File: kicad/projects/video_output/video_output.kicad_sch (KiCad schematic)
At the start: 70 parts, among them J1 peripheral_addr_bus_connector, J2 peripheral_aux_connector, J3 peripheral_membank_connector, J4 Conn_01x16_Socket, J5 Conn_01x16_Socket, J6 Conn_02x06_Odd_Even, J7 DE15_Receptacle_HighDensity, J8 video_aux, J9 Conn_01x04_Socket, U1 628128_DIP32_SSOP32, U10 74HC157, U11 74HC157, U12 74HC10, U13 74HC02, U14 74HC08, U15 74HC123, U16 74HC32, U17 74HC04, U2 628128_DIP32_SSOP32, U3 74HC245, U4 74HC245, U5 74HC245, U6 74HC245, U7 74HC574, U8 74HC245, U9 74HC574

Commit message: First pass of output PCB complete.
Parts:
- removed J7: DE15_Receptacle_HighDensity, Connector_Dsub:DSUB-15_Female_Horizontal_P2.77x2.84mm_EdgePinOffset9.90mm_Housed_MountingHolesOffset11.32mm, symbol Connector:DE15_Receptacle_HighDensity
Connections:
- net PIX_A_B_00: now also U2.14 (Q1), U3.14 (B5), U5.14 (B5); no longer U2.18 (Q4), U3.17 (B2), U5.17 (B2)
- net PIX_A_B_01: now also U2.13 (Q0), U3.13 (B6), U5.13 (B6); no longer U2.19 (Q5), U3.18 (B1), U5.18 (B1)
- net PIX_A_G_00: now also U2.17 (Q3), U3.16 (B3), U5.16 (B3); no longer U2.15 (Q2), U3.15 (B4), U5.15 (B4)
- net PIX_A_G_01: now also U2.15 (Q2), U3.15 (B4), U5.15 (B4); no longer U2.17 (Q3), U3.16 (B3), U5.16 (B3)
- net PIX_A_R_00: now also U2.19 (Q5), U3.18 (B1), U5.18 (B1); no longer U2.13 (Q0), U3.13 (B6), U5.13 (B6)
- net PIX_A_R_01: now also U2.18 (Q4), U3.17 (B2), U5.17 (B2); no longer U2.14 (Q1), U3.14 (B5), U5.14 (B5)
- net PIX_B_00: now also U9.18 (Q1); no longer U9.15 (Q4)
- net PIX_B_00_CLOCKED: now also RN5.8 (R7), U8.17 (B2), U9.3 (D1); no longer RN5.5 (R4), U8.14 (B5), U9.6 (D4)
- net PIX_B_00_OUT: now also R10.1, U8.3 (A2); no longer R14.1, U8.6 (A5)
- net PIX_B_01: now also U9.19 (Q0); no longer U9.14 (Q5)
- net PIX_B_01_CLOCKED: now also RN5.9 (R8), U8.18 (B1), U9.2 (D0); no longer RN5.4 (R3), U8.13 (B6), U9.7 (D5)
- net PIX_B_01_OUT: now also R11.1, U8.2 (A1); no longer R15.1, U8.7 (A6)
- net PIX_B_B_00: now also U1.14 (Q1), U4.14 (B5), U6.14 (B5); no longer U1.18 (Q4), U4.17 (B2), U6.17 (B2)
- net PIX_B_B_01: now also U1.13 (Q0), U4.13 (B6), U6.13 (B6); no longer U1.19 (Q5), U4.18 (B1), U6.18 (B1)
- net PIX_B_G_00: now also U1.17 (Q3), U4.16 (B3), U6.16 (B3); no longer U1.15 (Q2), U4.15 (B4), U6.15 (B4)
- net PIX_B_G_01: now also U1.15 (Q2), U4.15 (B4), U6.15 (B4); no longer U1.17 (Q3), U4.16 (B3), U6.16 (B3)
- net PIX_B_OUT: now also R10.2, R11.2; no longer R14.2, R15.2
- net PIX_B_R_00: now also U1.19 (Q5), U4.18 (B1), U6.18 (B1); no longer U1.13 (Q0), U4.13 (B6), U6.13 (B6)
- net PIX_B_R_01: now also U1.18 (Q4), U4.17 (B2), U6.17 (B2); no longer U1.14 (Q1), U4.14 (B5), U6.14 (B5)
- net PIX_G_00: now also U9.16 (Q3); no longer U9.17 (Q2)
- net PIX_G_00_CLOCKED: now also RN5.6 (R5), U8.15 (B4), U9.5 (D3); no longer RN5.7 (R6), U8.16 (B3), U9.4 (D2)
- net PIX_G_00_OUT: now also U8.5 (A3); no longer U8.4 (A3)
- net PIX_G_01: now also U9.17 (Q2); no longer U9.16 (Q3)
- net PIX_G_01_CLOCKED: now also RN5.7 (R6), U8.16 (B3), U9.4 (D2); no longer RN5.6 (R5), U8.15 (B4), U9.5 (D3)
- net PIX_G_01_OUT: now also U8.4 (A3); no longer U8.5 (A3)
- net PIX_R_00: now also U9.14 (Q5); no longer U9.19 (Q0)
- net PIX_R_00_CLOCKED: now also RN5.4 (R3), U8.13 (B6), U9.7 (D5); no longer RN5.9 (R8), U8.18 (B1), U9.2 (D0)
- net PIX_R_00_OUT: now also R14.1, U8.7 (A6); no longer R10.1, U8.2 (A1)
- net PIX_R_01: now also U9.15 (Q4); no longer U9.18 (Q1)
- net PIX_R_01_CLOCKED: now also RN5.5 (R4), U8.14 (B5), U9.6 (D4); no longer RN5.8 (R7), U8.17 (B2), U9.3 (D1)
- net PIX_R_01_OUT: now also R15.1, U8.6 (A5); no longer R11.1, U8.3 (A2)
- net PIX_R_OUT: now also R14.2, R15.2; no longer R10.2, R11.2
- net at RN2.2 (R1): now also U4.12 (B7); no longer U4.8 (A7)
- net at RN2.3 (R2): now also U4.11 (B8); no longer U4.9 (A8)
- net at RN2.4 (R3): now also U4.9 (A8); no longer U4.11 (B8)
- net at RN2.5 (R4): now also U4.8 (A7); no longer U4.12 (B7)
- net ~{SHORT_PULSE}: now reaches U14.13, U15.12 (~{Q})
- net LONG_PULSE: now reaches U14.12, U15.13 (Q)
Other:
- moved on the sheet: R10, R11, R12, R13, R14, R15

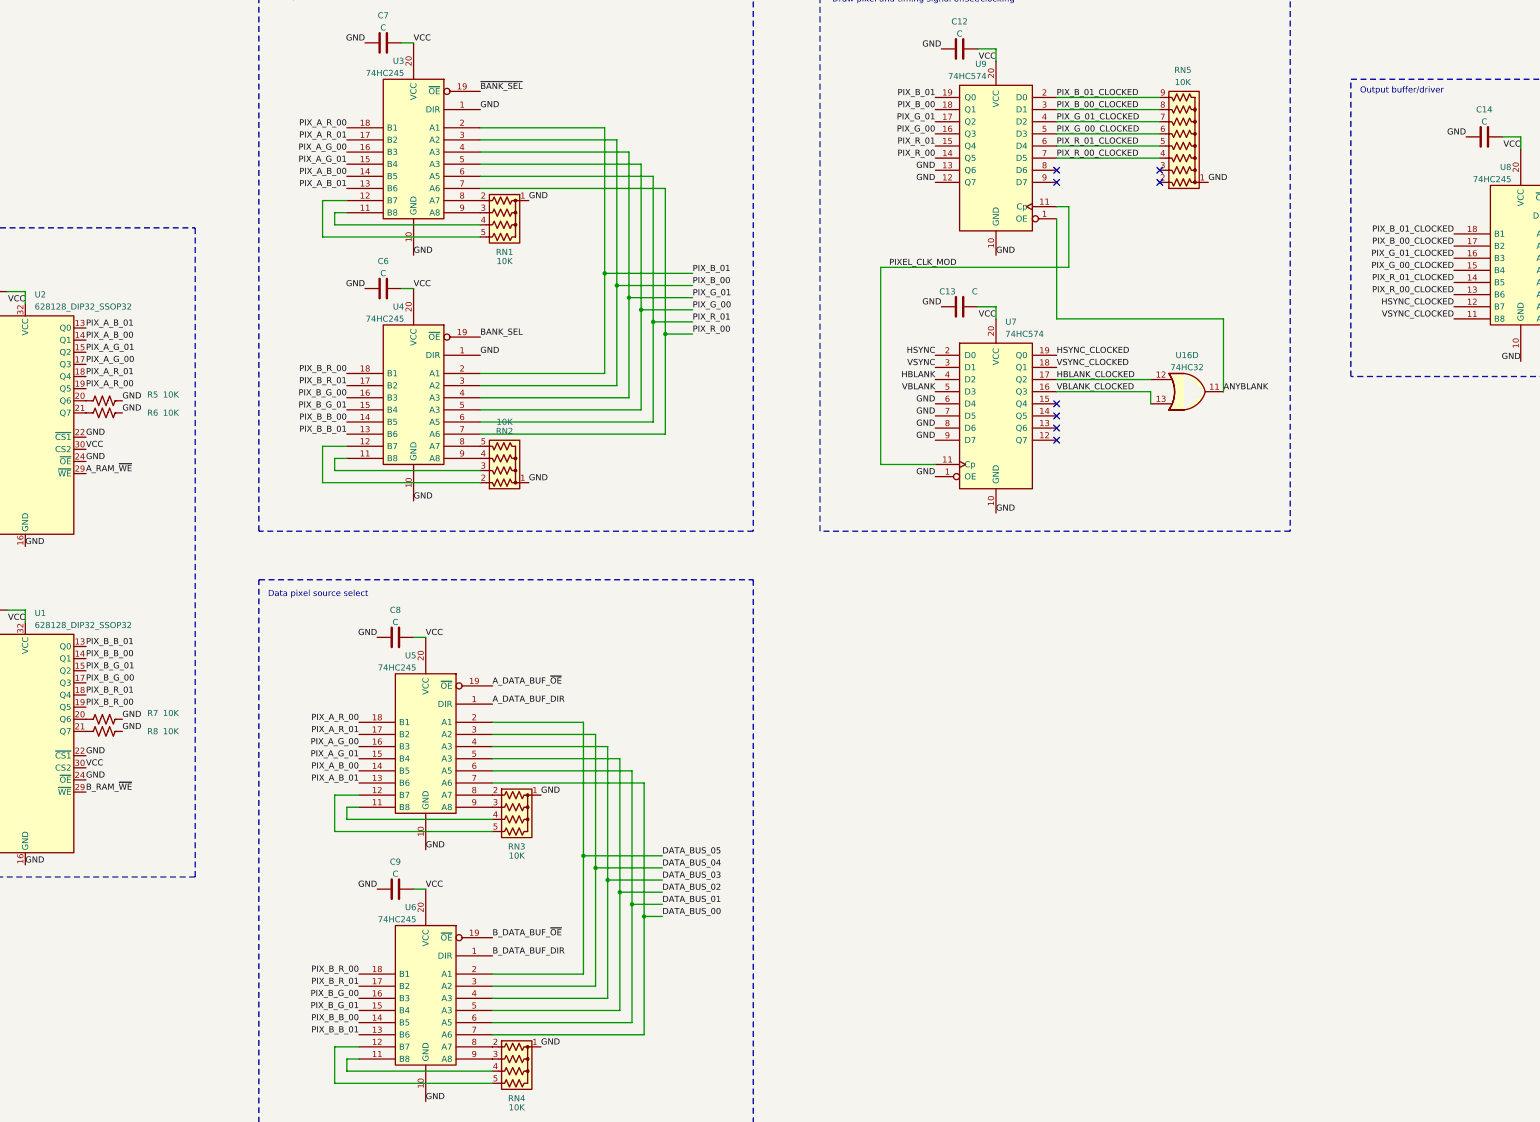
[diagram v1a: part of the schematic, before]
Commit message: Prep video out for RGB shuffle. Some work on shift status for tech checks, not complete yet.
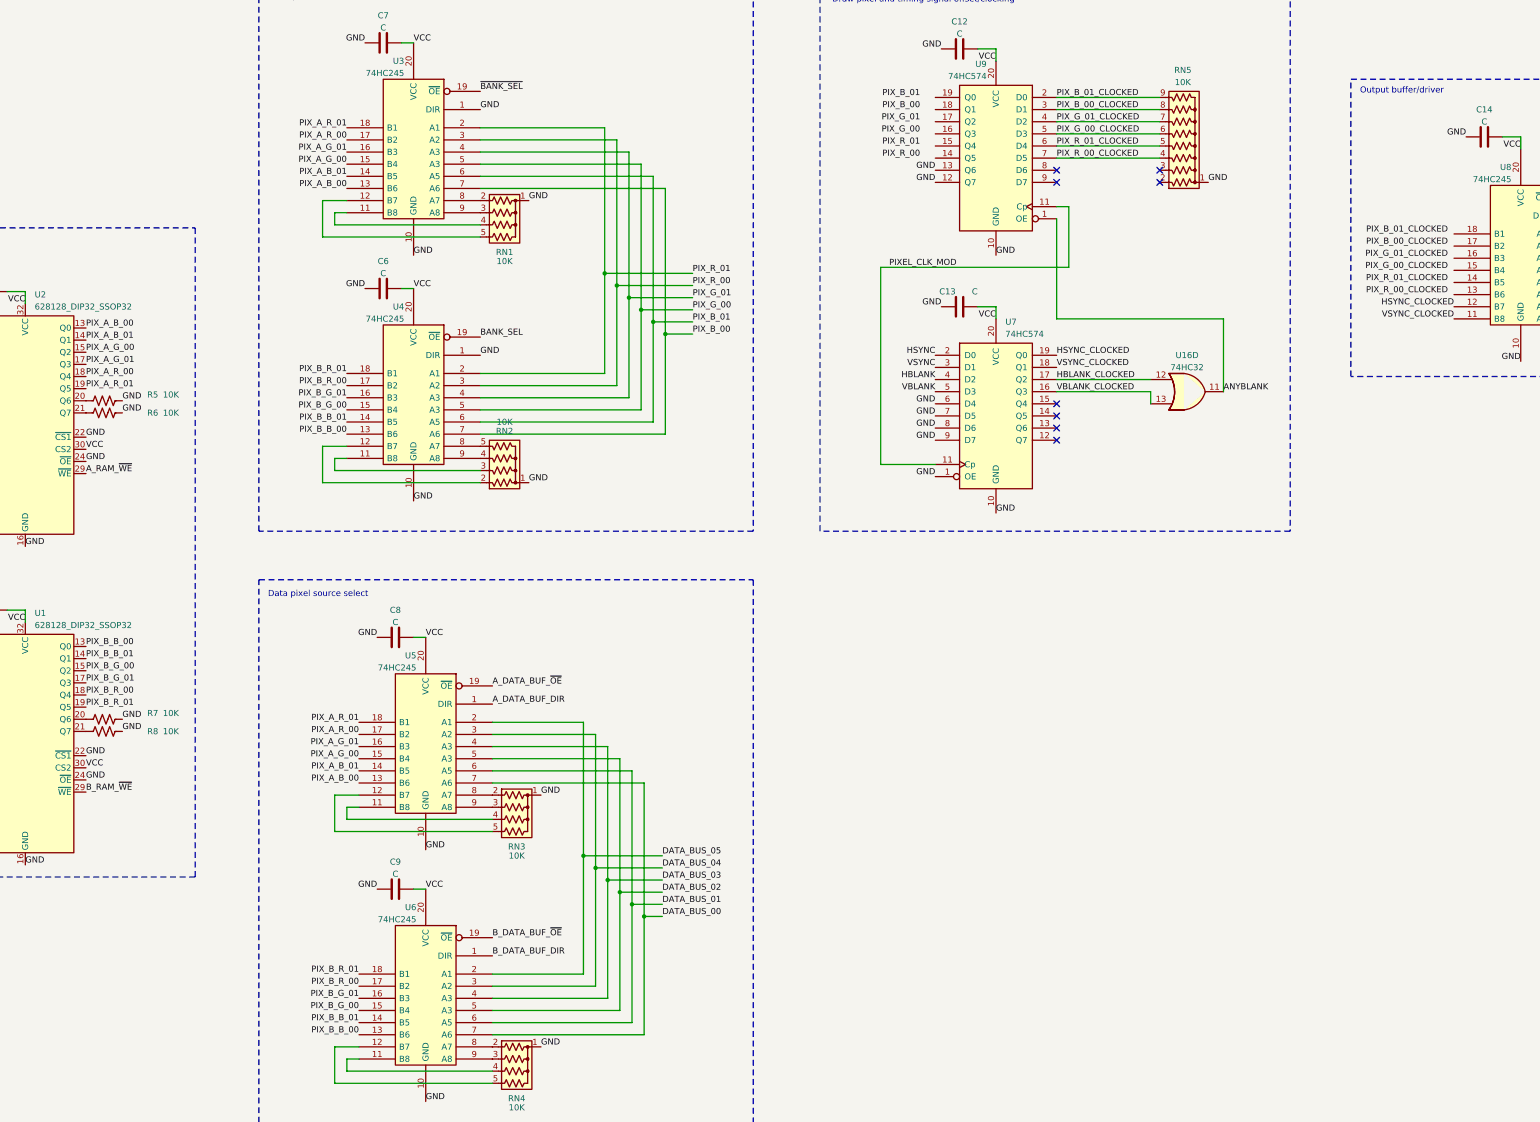
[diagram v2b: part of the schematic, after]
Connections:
- net PIX_A_B_00: now also U2.13 (Q0), U3.13 (B6), U5.13 (B6); no longer U2.14 (Q1), U3.14 (B5), U5.14 (B5)
- net PIX_A_B_01: now also U2.14 (Q1), U3.14 (B5), U5.14 (B5); no longer U2.13 (Q0), U3.13 (B6), U5.13 (B6)
- net PIX_A_G_00: now also U2.15 (Q2), U3.15 (B4), U5.15 (B4); no longer U2.17 (Q3), U3.16 (B3), U5.16 (B3)
- net PIX_A_G_01: now also U2.17 (Q3), U3.16 (B3), U5.16 (B3); no longer U2.15 (Q2), U3.15 (B4), U5.15 (B4)
- net PIX_A_R_00: now also U2.18 (Q4), U3.17 (B2), U5.17 (B2); no longer U2.19 (Q5), U3.18 (B1), U5.18 (B1)
- net PIX_A_R_01: now also U2.19 (Q5), U3.18 (B1), U5.18 (B1); no longer U2.18 (Q4), U3.17 (B2), U5.17 (B2)
- net PIX_B_00: now also U3.7 (A6), U4.7 (A6); no longer U3.3 (A2), U4.3 (A2), U9.18 (Q1)
- net PIX_B_00_CLOCKED: no longer U8.17 (B2)
- net PIX_B_01: now also U3.6 (A5), U4.6 (A5); no longer U3.2 (A1), U4.2 (A1), U9.19 (Q0)
- net PIX_B_01_CLOCKED: no longer U8.18 (B1)
- net PIX_B_B_00: now also U1.13 (Q0), U4.13 (B6), U6.13 (B6); no longer U1.14 (Q1), U4.14 (B5), U6.14 (B5)
- net PIX_B_B_01: now also U1.14 (Q1), U4.14 (B5), U6.14 (B5); no longer U1.13 (Q0), U4.13 (B6), U6.13 (B6)
- net PIX_B_G_00: now also U1.15 (Q2), U4.15 (B4), U6.15 (B4); no longer U1.17 (Q3), U4.16 (B3), U6.16 (B3)
- net PIX_B_G_01: now also U1.17 (Q3), U4.16 (B3), U6.16 (B3); no longer U1.15 (Q2), U4.15 (B4), U6.15 (B4)
- net PIX_B_R_00: now also U1.18 (Q4), U4.17 (B2), U6.17 (B2); no longer U1.19 (Q5), U4.18 (B1), U6.18 (B1)
- net PIX_B_R_01: now also U1.19 (Q5), U4.18 (B1), U6.18 (B1); no longer U1.18 (Q4), U4.17 (B2), U6.17 (B2)
- net PIX_G_00: no longer U9.16 (Q3)
- net PIX_G_00_CLOCKED: no longer U8.15 (B4)
- net PIX_G_01: no longer U9.17 (Q2)
- net PIX_G_01_CLOCKED: no longer U8.16 (B3)
- net PIX_R_00: now also U3.3 (A2), U4.3 (A2); no longer U3.7 (A6), U4.7 (A6), U9.14 (Q5)
- net PIX_R_00_CLOCKED: no longer U8.13 (B6)
- net PIX_R_01: now also U3.2 (A1), U4.2 (A1); no longer U3.6 (A5), U4.6 (A5), U9.15 (Q4)
- net PIX_R_01_CLOCKED: no longer U8.14 (B5)

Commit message: Switched A and B outputs on bank sel. Bit of work on logic and PCB for output. Clarified bank sel 0 and 1 and banks A and B in docs.
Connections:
- net DATA_BUF_DIR: now also U14.11, U16.1
- net GND: now also U17.9, U8.1 (DIR), U9.8 (D6), U9.9 (D7); no longer U9.12 (Q7), U9.13 (Q6)
- net PIX_B_00: now also U9.7 (D5)
- net PIX_B_00_CLOCKED: now also RN5.4 (R3), U8.13 (B6), U9.14 (Q5); no longer RN5.8 (R7), U9.3 (D1)
- net PIX_B_00_OUT: now also R14.1, U8.7 (A6); no longer R10.1, U8.3 (A2)
- net PIX_B_01: now also U9.6 (D4)
- net PIX_B_01_CLOCKED: now also RN5.5 (R4), U8.14 (B5), U9.15 (Q4); no longer RN5.9 (R8), U9.2 (D0)
- net PIX_B_01_OUT: now also R15.1, U8.6 (A5); no longer R11.1, U8.2 (A1)
- net PIX_B_OUT: now also R14.2, R15.2; no longer R10.2, R11.2
- net PIX_G_00: now also U9.5 (D3)
- net PIX_G_00_CLOCKED: now also U8.15 (B4), U9.16 (Q3); no longer U9.5 (D3)
- net PIX_G_01: now also U9.4 (D2)
- net PIX_G_01_CLOCKED: now also U8.16 (B3), U9.17 (Q2); no longer U9.4 (D2)
- net PIX_R_00: now also U9.3 (D1)
- net PIX_R_00_CLOCKED: now also RN5.8 (R7), U8.17 (B2), U9.18 (Q1); no longer RN5.4 (R3), U9.7 (D5)
- net PIX_R_00_OUT: now also R10.1, U8.3 (A2); no longer R14.1, U8.7 (A6)
- net PIX_R_01: now also U9.2 (D0)
- net PIX_R_01_CLOCKED: now also RN5.9 (R8), U8.18 (B1), U9.19 (Q0); no longer RN5.5 (R4), U9.6 (D4)
- net PIX_R_01_OUT: now also R11.1, U8.2 (A1); no longer R15.1, U8.6 (A5)
- net PIX_R_OUT: now also R10.2, R11.2; no longer R14.2, R15.2
- net R/~{W}: now reaches U12.11, U12.12
- no-connect marks 65 -> 66
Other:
- note removed: "May or may not need this depending on buffer orientataion"
- moved on the sheet: U17D

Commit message: Switch bank A and B positions on output and bank sel. Video output PCB mostly done.
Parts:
- removed C1: C, Capacitor_THT:C_Disc_D5.0mm_W2.5mm_P5.00mm, symbol Device:C
- removed R1: R_US, Resistor_THT:R_Axial_DIN0207_L6.3mm_D2.5mm_P10.16mm_Horizontal, symbol Device:R_US
- removed TP1: TestPoint, Connector_Pin:Pin_D1.0mm_L10.0mm, symbol Connector:TestPoint
- C97, C98, C99: value C_Polarized -> 33uF
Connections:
- net A_DATA_BUF_DIR: now also U10.7 (2Y), U6.1 (DIR); no longer U11.7 (2Y), U5.1 (DIR)
- net A_DATA_BUF_~{OE}: now also U10.4 (1Y), U6.19 (~{OE}); no longer U11.4 (1Y), U5.19 (~{OE})
- net A_RAM_~{WE}: now also U1.29 (~{WE}), U10.9 (3Y); no longer U11.9 (3Y), U2.29 (~{WE})
- net BANK_SEL: now also U10.1 (~{A}/B), U3.19 (~{OE}); no longer U11.1 (~{A}/B), U4.19 (~{OE})
- net B_DATA_BUF_DIR: now also U11.7 (2Y), U5.1 (DIR); no longer U10.7 (2Y), U6.1 (DIR)
- net B_DATA_BUF_~{OE}: now also U11.4 (1Y), U5.19 (~{OE}); no longer U10.4 (1Y), U6.19 (~{OE})
- net B_RAM_~{WE}: now also U11.9 (3Y), U2.29 (~{WE}); no longer U1.29 (~{WE}), U10.9 (3Y)
- net COL_A_00: now also J4.1 (Pin_1), U1.12 (A0); no longer J5.1 (Pin_1), U2.12 (A0)
- net COL_A_01: now also J4.2 (Pin_2), U1.11 (A1); no longer J5.2 (Pin_2), U2.11 (A1)
- net COL_A_02: now also J4.3 (Pin_3), U1.10 (A2); no longer J5.3 (Pin_3), U2.10 (A2)
- net COL_A_03: now also J4.4 (Pin_4), U1.9 (A3); no longer J5.4 (Pin_4), U2.9 (A3)
- net COL_A_04: now also J4.5 (Pin_5), U1.8 (A4); no longer J5.5 (Pin_5), U2.8 (A4)
- net COL_A_05: now also J4.6 (Pin_6), U1.7 (A5); no longer J5.6 (Pin_6), U2.7 (A5)
- net COL_A_06: now also J4.7 (Pin_7), U1.6 (A6); no longer J5.7 (Pin_7), U2.6 (A6)
- net COL_A_07: now also J4.8 (Pin_8), U1.5 (A7); no longer J5.8 (Pin_8), U2.5 (A7)
- net COL_B_00: now also J5.1 (Pin_1), U2.12 (A0); no longer J4.1 (Pin_1), U1.12 (A0)
- net COL_B_01: now also J5.2 (Pin_2), U2.11 (A1); no longer J4.2 (Pin_2), U1.11 (A1)
- net COL_B_02: now also J5.3 (Pin_3), U2.10 (A2); no longer J4.3 (Pin_3), U1.10 (A2)
- net COL_B_03: now also J5.4 (Pin_4), U2.9 (A3); no longer J4.4 (Pin_4), U1.9 (A3)
- net COL_B_04: now also J5.5 (Pin_5), U2.8 (A4); no longer J4.5 (Pin_5), U1.8 (A4)
- net COL_B_05: now also J5.6 (Pin_6), U2.7 (A5); no longer J4.6 (Pin_6), U1.7 (A5)
- net COL_B_06: now also J5.7 (Pin_7), U2.6 (A6); no longer J4.7 (Pin_7), U1.6 (A6)
- net COL_B_07: now also J5.8 (Pin_8), U2.5 (A7); no longer J4.8 (Pin_8), U1.5 (A7)
- net GND: now also C3.2, U15.6 (Cext); no longer RN1.1 (common), RN2.1 (common)
- net PIX_A_B_00: now also U1.13 (Q0), U4.13 (B6), U6.13 (B6); no longer U2.13 (Q0), U3.13 (B6), U5.13 (B6)
- net PIX_A_B_01: now also U1.14 (Q1), U4.14 (B5), U6.14 (B5); no longer U2.14 (Q1), U3.14 (B5), U5.14 (B5)
- net PIX_A_G_00: now also U1.15 (Q2), U4.15 (B4), U6.15 (B4); no longer U2.15 (Q2), U3.15 (B4), U5.15 (B4)
- net PIX_A_G_01: now also U1.17 (Q3), U4.16 (B3), U6.16 (B3); no longer U2.17 (Q3), U3.16 (B3), U5.16 (B3)
- net PIX_A_R_00: now also U1.18 (Q4), U4.17 (B2), U6.17 (B2); no longer U2.18 (Q4), U3.17 (B2), U5.17 (B2)
- net PIX_A_R_01: now also U1.19 (Q5), U4.18 (B1), U6.18 (B1); no longer U2.19 (Q5), U3.18 (B1), U5.18 (B1)
- net PIX_B_B_00: now also U2.13 (Q0), U3.13 (B6), U5.13 (B6); no longer U1.13 (Q0), U4.13 (B6), U6.13 (B6)
- net PIX_B_B_01: now also U2.14 (Q1), U3.14 (B5), U5.14 (B5); no longer U1.14 (Q1), U4.14 (B5), U6.14 (B5)
- net PIX_B_G_00: now also U2.15 (Q2), U3.15 (B4), U5.15 (B4); no longer U1.15 (Q2), U4.15 (B4), U6.15 (B4)
- net PIX_B_G_01: now also U2.17 (Q3), U3.16 (B3), U5.16 (B3); no longer U1.17 (Q3), U4.16 (B3), U6.16 (B3)
- net PIX_B_R_00: now also U2.18 (Q4), U3.17 (B2), U5.17 (B2); no longer U1.18 (Q4), U4.17 (B2), U6.17 (B2)
- net PIX_B_R_01: now also U2.19 (Q5), U3.18 (B1), U5.18 (B1); no longer U1.19 (Q5), U4.18 (B1), U6.18 (B1)
- net ROW_A_00: now also J4.9 (Pin_9), U1.27 (A8); no longer J5.9 (Pin_9), U2.27 (A8)
- net ROW_A_01: now also J4.10 (Pin_10), U1.26 (A9); no longer J5.10 (Pin_10), U2.26 (A9)
- net ROW_A_02: now also J4.11 (Pin_11), U1.23 (A10); no longer J5.11 (Pin_11), U2.23 (A10)
- net ROW_A_03: now also J4.12 (Pin_12), U1.25 (A11); no longer J5.12 (Pin_12), U2.25 (A11)
- net ROW_A_04: now also J4.13 (Pin_13), U1.4 (A12); no longer J5.13 (Pin_13), U2.4 (A12)
- net ROW_A_05: now also J4.14 (Pin_14), U1.28 (A13); no longer J5.14 (Pin_14), U2.28 (A13)
- net ROW_A_06: now also J4.15 (Pin_15), U1.3 (A14); no longer J5.15 (Pin_15), U2.3 (A14)
- net ROW_B_00: now also J5.9 (Pin_9), U2.27 (A8); no longer J4.9 (Pin_9), U1.27 (A8)
- net ROW_B_01: now also J5.10 (Pin_10), U2.26 (A9); no longer J4.10 (Pin_10), U1.26 (A9)
- net ROW_B_02: now also J5.11 (Pin_11), U2.23 (A10); no longer J4.11 (Pin_11), U1.23 (A10)
- net ROW_B_03: now also J5.12 (Pin_12), U2.25 (A11); no longer J4.12 (Pin_12), U1.25 (A11)
- net ROW_B_04: now also J5.13 (Pin_13), U2.4 (A12); no longer J4.13 (Pin_13), U1.4 (A12)
- net ROW_B_05: now also J5.14 (Pin_14), U2.28 (A13); no longer J4.14 (Pin_14), U1.28 (A13)
- net ROW_B_06: now also J5.15 (Pin_15), U2.3 (A14); no longer J4.15 (Pin_15), U1.3 (A14)
- net ~{BANK_SEL}: now also U11.1 (~{A}/B), U4.19 (~{OE}); no longer U10.1 (~{A}/B), U3.19 (~{OE})
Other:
- moved on the sheet: C10, C11, C12, C13, C14, C15, C16, C17, C18, C19, C2, C20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

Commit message: Video output tech checks complete
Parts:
- added J10: DATA_BUF_DIR, Connector_PinHeader_2.54mm:PinHeader_1x02_P2.54mm_Vertical, symbol Connector:Conn_01x02_Pin
- added J11: DATA_BUF_~{OE}, Connector_PinHeader_2.54mm:PinHeader_1x02_P2.54mm_Vertical, symbol Connector:Conn_01x02_Pin
- added J12: LONG_PULSE, Connector_PinHeader_2.54mm:PinHeader_1x02_P2.54mm_Vertical, symbol Connector:Conn_01x02_Pin
- added J13: ~{SHORT_PULSE}, Connector_PinHeader_2.54mm:PinHeader_1x02_P2.54mm_Vertical, symbol Connector:Conn_01x02_Pin
- added J14: GND, Connector_PinHeader_2.54mm:PinHeader_1x02_P2.54mm_Vertical, symbol Connector:Conn_01x02_Pin
- added J15: SAFE_CLK, Connector_PinHeader_2.54mm:PinHeader_1x02_P2.54mm_Vertical, symbol Connector:Conn_01x02_Pin
- added J7: RAM_~{WE}, Connector_PinHeader_2.54mm:PinHeader_1x02_P2.54mm_Vertical, symbol Connector:Conn_01x02_Pin
- added R1, R9: 10K, Resistor_THT:R_Axial_DIN0207_L6.3mm_D2.5mm_P10.16mm_Horizontal, symbol Device:R_US
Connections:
- net A_DATA_BUF_~{OE}: now also R1.2
- net B_DATA_BUF_~{OE}: now also R9.2
- net DATA_BUF_DIR: now also J10.1 (Pin_1), J10.2 (Pin_2)
- net DATA_BUF_~{OE}: now also J11.1 (Pin_1), J11.2 (Pin_2)
- net GND: now also RN1.1 (common), RN2.1 (common), J14.2 (Pin_2)
- net LONG_PULSE: now also J12.1 (Pin_1), J12.2 (Pin_2)
- net RAM_~{WE}: now also J7.1 (Pin_1), J7.2 (Pin_2)
- net SAFE_CLK: now also J15.1 (Pin_1), J15.2 (Pin_2)
- net VCC: now also R1.1, R9.1
- net ~{SHORT_PULSE}: now also J13.1 (Pin_1), J13.2 (Pin_2)
- net ~{ADDRESSED_RFM}: no longer names the net of U12.8, U17.11
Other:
- moved on the sheet: C2, C3, R2, R3, R4, U14D, U15A, U15B, U16A, U17F
